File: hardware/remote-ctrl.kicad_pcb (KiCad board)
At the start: 2 copper layers, 1 part, among them IC1 STM32G030K8T6

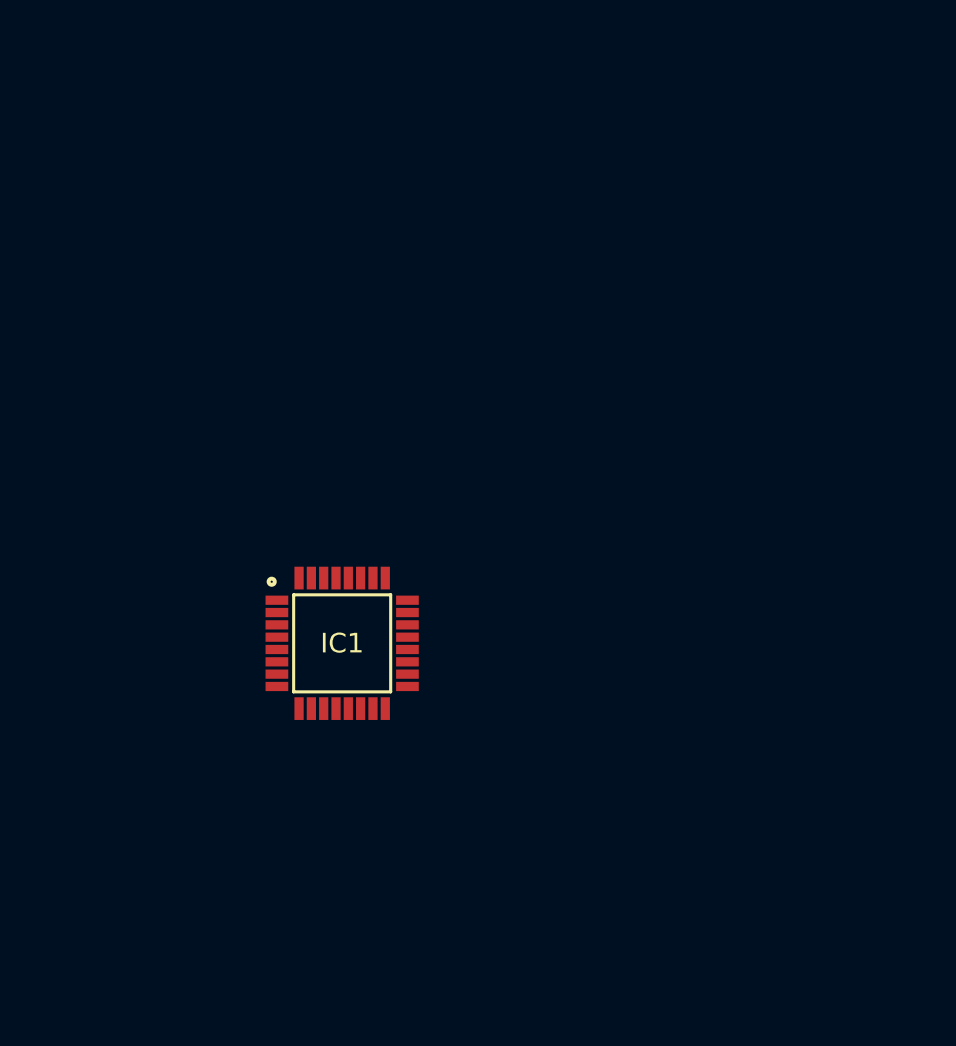
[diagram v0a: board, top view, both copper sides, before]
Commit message: Added external port, some pin remaped, initial PCB
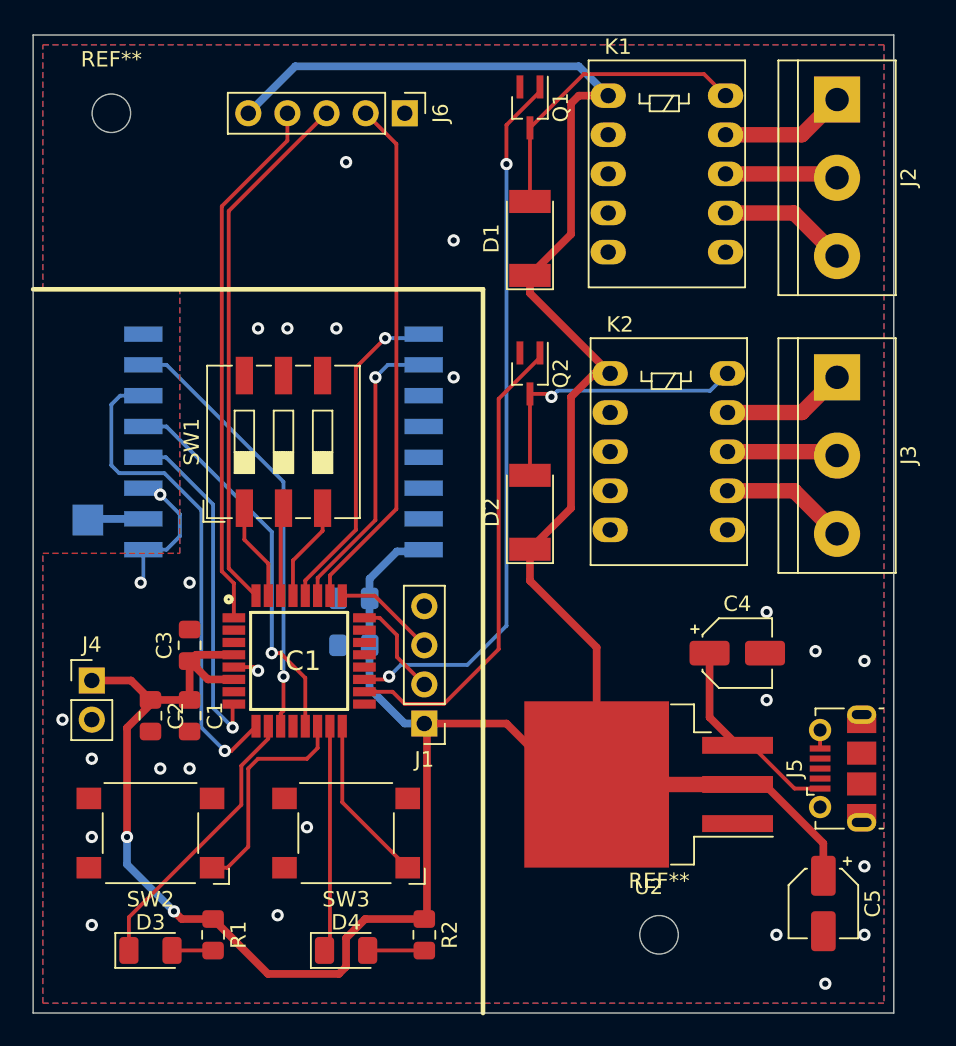
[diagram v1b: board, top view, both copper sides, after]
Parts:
- added AE1: Antenna, TestPoint:TestPoint_Pad_2.0x2.0mm, B.Cu at (29.0, 69.6)
- added C1: 100nF, Capacitor_SMD:C_0805_2012Metric_Pad1.15x1.40mm_HandSolder, F.Cu at (35.6, 82.3)
- added C2: 4.7uF, Capacitor_SMD:C_0805_2012Metric_Pad1.15x1.40mm_HandSolder, F.Cu at (33.0, 82.3)
- added C3: 100nF, Capacitor_SMD:C_0805_2012Metric_Pad1.15x1.40mm_HandSolder, F.Cu at (35.6, 77.7)
- added C4: 10uF, Capacitor_SMD:CP_Elec_4x5.3, F.Cu at (71.1, 78.2)
- added C5: 10uF, Capacitor_SMD:CP_Elec_4x5.3, F.Cu at (76.7, 94.5)
- added C6: 100nF, Capacitor_SMD:C_0805_2012Metric_Pad1.15x1.40mm_HandSolder, B.Cu at (46.2, 77.7)
- added C7: 1uF, Capacitor_SMD:C_0805_2012Metric_Pad1.15x1.40mm_HandSolder, B.Cu at (46.2, 74.7)
- added D1: D_Schottky, Diode_SMD:D_MELF, F.Cu at (57.7, 51.3)
- added D2: D_Schottky, Diode_SMD:D_MELF, F.Cu at (57.7, 69.1)
- added D3: LED, Diode_SMD:D_1206_3216Metric, F.Cu at (33.0, 97.5)
- added D4: LED, Diode_SMD:D_1206_3216Metric, F.Cu at (45.7, 97.5)
- added J1: PRG, Connector_PinHeader_2.54mm:PinHeader_1x04_P2.54mm_Vertical, F.Cu at (50.8, 82.8)
- added J2: CON-1, TerminalBlock:TerminalBlock_bornier-3_P5.08mm, F.Cu at (77.6, 42.3)
- added J3: CON-2, TerminalBlock:TerminalBlock_bornier-3_P5.08mm, F.Cu at (77.6, 60.3)
- added J4: BATT, Connector_PinHeader_2.54mm:PinHeader_1x02_P2.54mm_Vertical, F.Cu at (29.2, 80.0)
- added J5: USB_B_Micro, Connector_USB:USB_Micro-B_Molex-105017-0001, F.Cu at (78.0, 85.7)
- added J6: EXTERNAL, Connector_PinHeader_2.54mm:PinHeader_1x05_P2.54mm_Vertical, F.Cu at (49.5, 43.2)
- added K1: AZ822-2C-3DSE, Relay_THT:Relay_DPDT_FRT5, F.Cu at (62.7, 42.0)
- added K2: AZ822-2C-3DSE, Relay_THT:Relay_DPDT_FRT5, F.Cu at (62.9, 60.1)
- added Q1: PDTC114EU, Package_TO_SOT_SMD:SOT-323_SC-70_Handsoldering, F.Cu at (57.7, 42.8)
- added Q2: PDTC114EU, Package_TO_SOT_SMD:SOT-323_SC-70_Handsoldering, F.Cu at (57.7, 60.1)
- added R1: R_Small, Resistor_SMD:R_0805_2012Metric_Pad1.15x1.40mm_HandSolder, F.Cu at (37.1, 96.5)
- added R2: R_Small, Resistor_SMD:R_0805_2012Metric_Pad1.15x1.40mm_HandSolder, F.Cu at (50.8, 96.5)
- added REF**: MountingHole_2.5mm, MountingHole:MountingHole_2.5mm, F.Cu at (66.0, 96.5)
- added REF**: MountingHole_2.5mm, MountingHole:MountingHole_2.5mm, F.Cu at (30.5, 43.2)
- added SW1: ESD103EZ, Button_Switch_SMD:SW_DIP_SPSTx03_Slide_9.78x9.8mm_W8.61mm_P2.54mm, F.Cu at (41.7, 64.5)
- added SW2: BTN1, Button_Switch_SMD:SW_SPST_Omron_B3FS-101xP, F.Cu at (33.0, 89.9)
- added SW3: BTN2, Button_Switch_SMD:SW_SPST_Omron_B3FS-101xP, F.Cu at (45.7, 89.9)
- added U1: RFM69HW-868S2, RF_Module:HOPERF_RFM69HW, B.Cu at (41.7, 64.5)
- added U2: LD1085D2T33R, Package_TO_SOT_SMD:TO-263-3_TabPin2, F.Cu at (65.4, 86.8)
- moved IC1 3.02 mm to (42.7, 78.7)
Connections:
- IC1 pad 1: Net-(IC1-Pad1) -> /EXT-1
- IC1 pad 10: Net-(IC1-Pad10) -> /LED-1
- IC1 pad 11: Net-(IC1-Pad11) -> /NSS
- IC1 pad 13: Net-(IC1-Pad13) -> /MISO
- IC1 pad 14: Net-(IC1-Pad14) -> /BTN-1
- IC1 pad 15: Net-(IC1-Pad15) -> /LED-2
- IC1 pad 16: Net-(IC1-Pad16) -> /BTN-2
- IC1 pad 18: Net-(IC1-Pad18) -> /RELAY-2
- IC1 pad 19: Net-(IC1-Pad19) -> /RELAY-1
- IC1 pad 24: Net-(IC1-Pad24) -> /SWDIO
- IC1 pad 25: Net-(IC1-Pad25) -> /SWCLK
- IC1 pad 26: Net-(IC1-Pad26) -> /EXT-3
- IC1 pad 27: Net-(IC1-Pad27) -> /RF_IRQ
- IC1 pad 28: Net-(IC1-Pad28) -> /RF_RST
- IC1 pad 29: Net-(IC1-Pad29) -> /CODE-3
- IC1 pad 30: Net-(IC1-Pad30) -> /CODE-2
- IC1 pad 31: Net-(IC1-Pad31) -> /CODE-1
- IC1 pad 32: Net-(IC1-Pad32) -> /EXT-2
- IC1 pad 4: Net-(IC1-Pad4) -> VDD
- IC1 pad 5: Net-(IC1-Pad5) -> GND
- IC1 pad 6: Net-(IC1-Pad6) -> VDD
- IC1 pad 8: Net-(IC1-Pad8) -> /SCK
- IC1 pad 9: Net-(IC1-Pad9) -> /MOSI
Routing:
- net VDD: track 0.00 -> 192.0 mm, vias 0 -> 2
- net /RELAY-1: track 0.00 -> 46.6 mm, vias 0 -> 2
- net /EXT-1: track 0.00 -> 34.8 mm
- net /EXT-2: track 0.00 -> 34.7 mm
- net /EXT-3: track 0.00 -> 33.9 mm
- net /MOSI: track 0.00 -> 32.3 mm, vias 0 -> 1
- net /RELAY-2: track 0.00 -> 30.9 mm
- net /NSS: track 0.00 -> 28.2 mm, vias 0 -> 1
- net /MISO: track 0.00 -> 25.0 mm, vias 0 -> 1
- net /SCK: track 0.00 -> 22.4 mm, vias 0 -> 1
- net /RF_RST: track 0.00 -> 21.5 mm, vias 0 -> 1
- net Net-(D1-Pad2): track 0.00 -> 19.5 mm
- net /RF_IRQ: track 0.00 -> 19.2 mm, vias 0 -> 1
- net Net-(D2-Pad2): track 0.00 -> 18.8 mm, vias 0 -> 1
- net /LED-1: track 0.00 -> 18.3 mm
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- added copper zone on B.Cu, net GND
- added copper zone on F.Cu, net GND
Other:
- board outline added: 55.9 x 63.5 mm
- net class 230AC added: clearance 1, trace_width 1, via_dia 1, via_drill 0.8
